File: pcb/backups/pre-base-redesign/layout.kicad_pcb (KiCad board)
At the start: 2 copper layers, 36 x 86 mm, 43 parts, among them J1 B2B-PH-K-S, J2 BM02B-SRSS-TB(LF)(SN), J3 B2B-PH-K-S, Q1 AO3400A, SW1 PTS841GKSMTR LFS, SW2 JS202011AQN, U1 113991115, U2 MAX98357AETE+T, U3 MAX17048G+T10, U4 BMI270, U5 PCA9685PW,118, U6 AP2112K-3.3TRG1

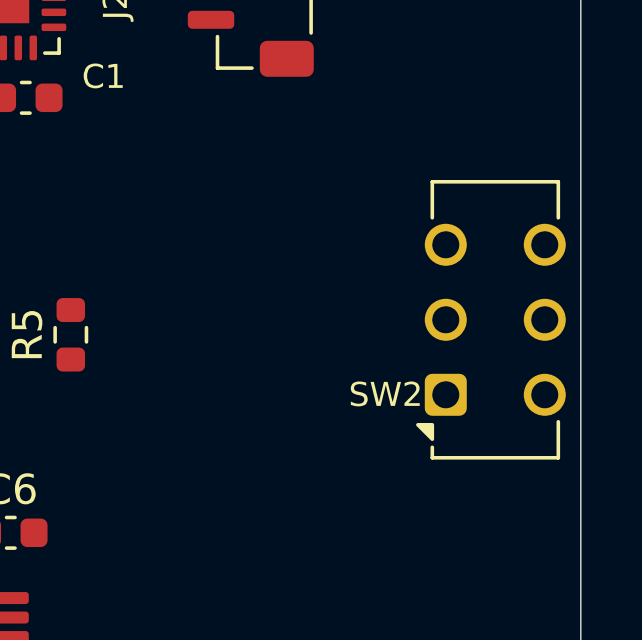
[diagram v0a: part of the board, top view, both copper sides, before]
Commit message: Add comprehensive BOM and redesign documentation for new components
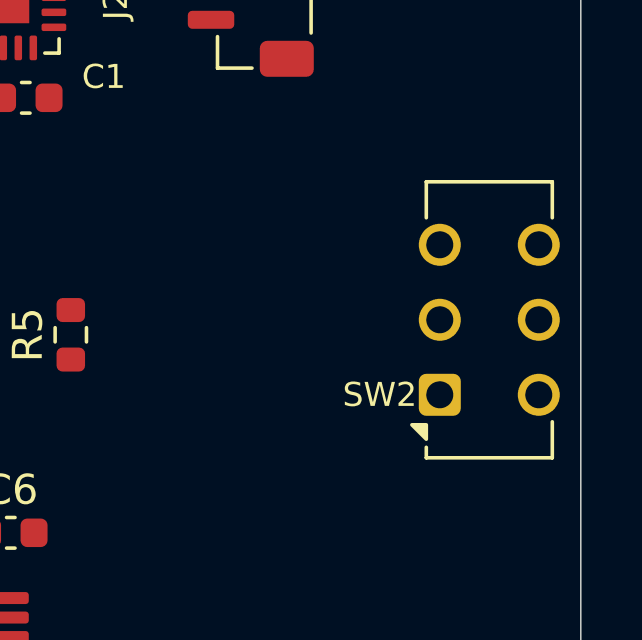
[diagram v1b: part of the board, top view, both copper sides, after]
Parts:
- moved SW2 0.20 mm to (113.3, 86.0)
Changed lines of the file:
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@@
 		(locked yes)
 		(layer "F.Cu")
-		(at 113.5 86 90)
+		(at 113.3 86 90)
 		(descr "C&K sub miniature slide switch, JS series, DPDT, right angle, http://www.ckswitches.com/media/1422/js.pdf")
 		(tags "switch DPDT")
